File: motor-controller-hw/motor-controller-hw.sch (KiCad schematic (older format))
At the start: 37 parts, among them J101 CAN, J102 Throttle, J103 Motor T, J104 Tran T, J105 USB_B_Micro, J106 Extra IO, J107 Hall Sensors, J108 CAN_DBG, J109 ABN Encoder, J110 SPI_DBG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

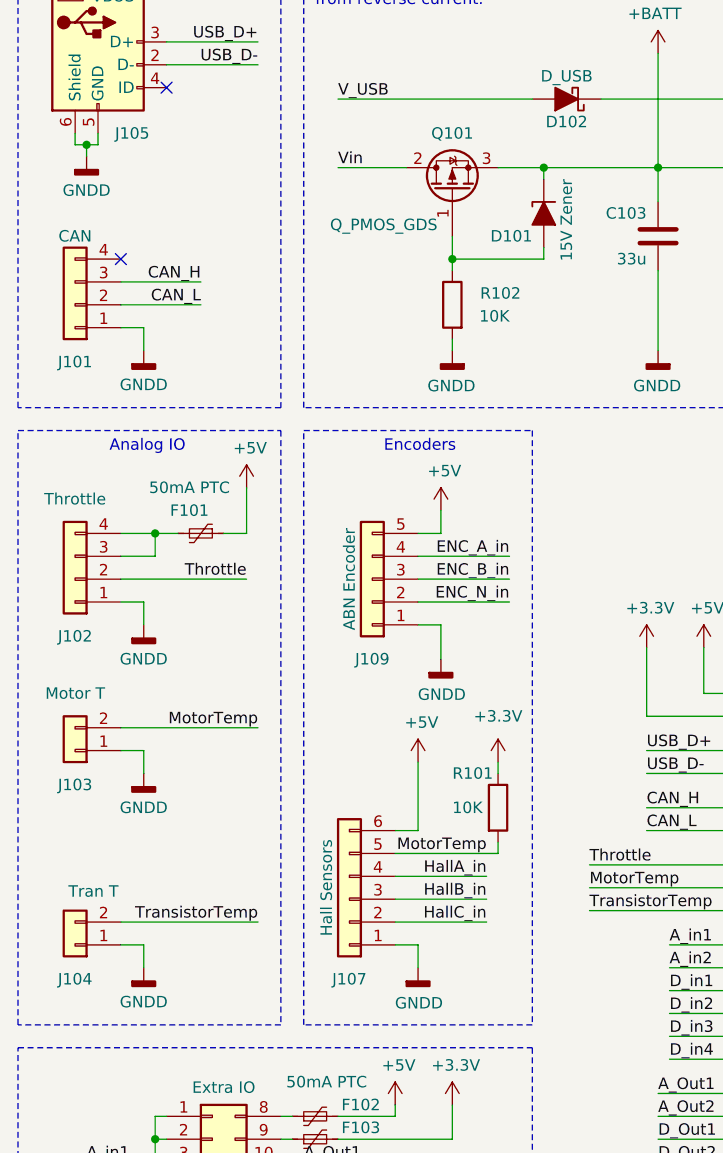
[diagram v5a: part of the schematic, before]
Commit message: PCB rev 1.1 -Fixed the TMC4671 footprint (use the Digi-Key layout) -Fixed the USB pull up issue for using the DFU bootloader -Fixed the orientation of the Hall sensor connector -Added a PTC on the hall effect sensor line -Added a 5v jumper for the CAN port
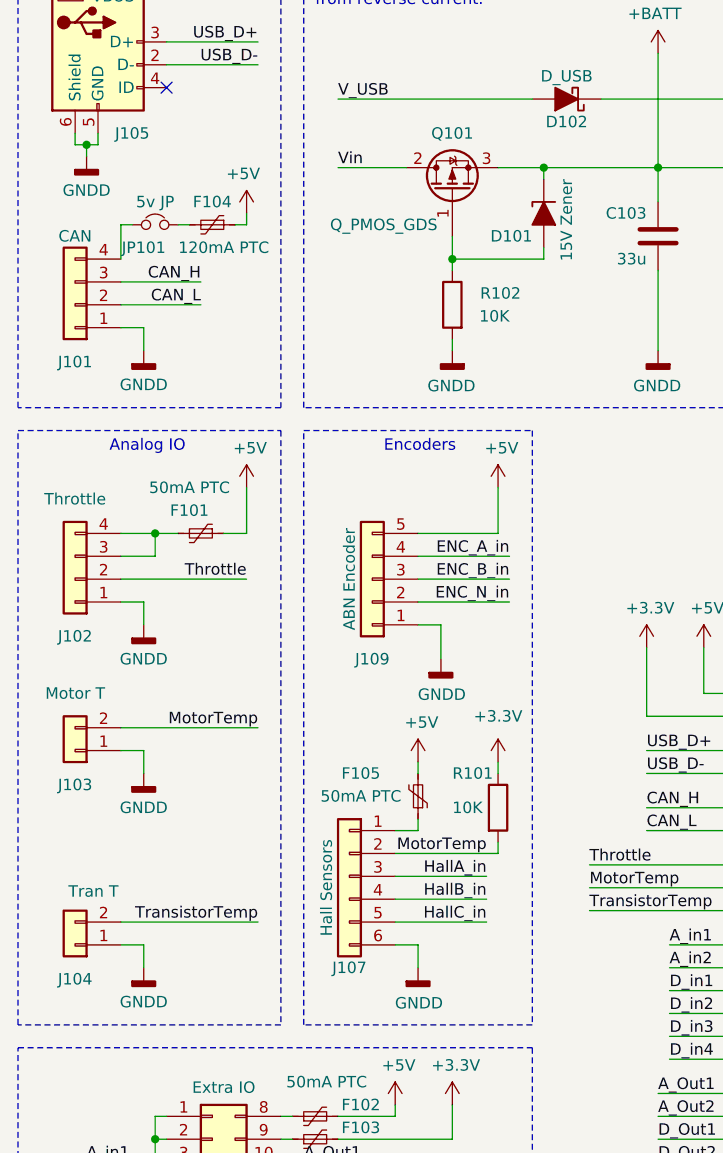
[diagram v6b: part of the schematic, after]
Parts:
- added F104: 120mA PTC, Fuse:Fuse_0603_1608Metric_Pad1.05x0.95mm_HandSolder, symbol MotorControllerParts:Polyfuse_Small
- added F105: 50mA PTC, Fuse:Fuse_0603_1608Metric_Pad1.05x0.95mm_HandSolder, symbol MotorControllerParts:Polyfuse_Small
- added JP101: 5v JP, Connector_PinHeader_2.54mm:PinHeader_1x02_P2.54mm_Vertical, symbol MotorControllerParts:Jumper_NC_Small
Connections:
- net +5V: now also F104.1, F105.2; no longer J107.6 (Pin_6)
- net GNDD: now also J107.6 (Pin_6); no longer J107.1 (Pin_1)
- net HallA_in: now also J107.3 (Pin_3); no longer J107.4 (Pin_4)
- net HallB_in: now also J107.4 (Pin_4); no longer J107.3 (Pin_3)
- net HallC_in: now also J107.5 (Pin_5); no longer J107.2 (Pin_2)
- net MotorTemp: now also J107.2 (Pin_2); no longer J107.5 (Pin_5)
- net at J101.4 (Pin_4): now also JP101.1
- new net: F105.1, J107.1 (Pin_1)
- new net: F104.2, JP101.2
- no-connect marks 22 -> 21
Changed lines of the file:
@@
 Wire Wire Line
 	1600 1300 1200 1300
-NoConn ~ 1000 2150
 $Comp
 L MotorControllerParts:Polyfuse_Small F101
@@
 L MotorControllerParts:Conn_01x06 J107
 U 1 1 5BF7BB3E
-P 2000 4950
-F 0 "J107" H 2000 5300 50  0000 C CNN
-F 1 "Hall Sensors" V 2100 4900 50  0000 C CNN
-F 2 "supermileage_footprints:MICRO_JST_6" H 2000 4950 50  0001 C CNN
-F 3 "http://www.jst-mfg.com/product/pdf/eng/ePH.pdf" H 2000 4950 50  0001 C CNN
-F 4 "455-1708-ND" H 2000 4950 50  0001 C CNN "Digi-key#"
-	1    2000 4950
-	-1   0    0    1
+P 2000 4850
+F 0 "J107" H 2000 4450 50  0000 C CNN
+F 1 "Hall Sensors" V 2100 4800 50  0000 C CNN
+F 2 "supermileage_footprints:MICRO_JST_6" H 2000 4850 50  0001 C CNN
+F 3 "http://www.jst-mfg.com/product/pdf/eng/ePH.pdf" H 2000 4850 50  0001 C CNN
+F 4 "455-1708-ND" H 2000 4850 50  0001 C CNN "Digi-key#"
+	1    2000 4850
+	-1   0    0    -1
 $EndComp
 $Comp
@@
 	1    0    0    -1
 $EndComp
-Wire Wire Line
-	2300 4350 2300 4650
 Wire Wire Line
 	2300 4650 2200 4650
@@
 L MotorControllerParts:+5V #PWR0118
 U 1 1 5E78636F
-P 2400 3250
-F 0 "#PWR0118" H 2400 3100 50  0001 C CNN
-F 1 "+5V" H 2415 3423 50  0000 C CNN
-F 2 "" H 2400 3250 50  0001 C CNN
-F 3 "" H 2400 3250 50  0001 C CNN
-	1    2400 3250
-	1    0    0    -1
-$EndComp
-Wire Wire Line
-	2400 3250 2400 3350
-Wire Wire Line
-	2400 3350 2300 3350
+P 2650 3150
+F 0 "#PWR0118" H 2650 3000 50  0001 C CNN
+F 1 "+5V" H 2665 3323 50  0000 C CNN
+F 2 "" H 2650 3150 50  0001 C CNN
+F 3 "" H 2650 3150 50  0001 C CNN
+	1    2650 3150
+	1    0    0    -1
+$EndComp
 Wire Wire Line
 	2400 3900 2400 3750
@@
 Power Status LEDs
 NoConn ~ 9900 1750
+$Comp
+L MotorControllerParts:Polyfuse_Small F104
+U 1 1 5CA283F1
+P 1400 2000
+F 0 "F104" V 1300 2000 50  0000 C CNN
+F 1 "120mA PTC" V 1500 2050 50  0000 C CNN
+F 2 "Fuse:Fuse_0603_1608Metric_Pad1.05x0.95mm_HandSolder" H 1450 1800 50  0001 L CNN
+F 3 "https://belfuse.com/resources/CircuitProtection/datasheets/0ZCM%20Nov2016.pdf" H 1400 2000 50  0001 C CNN
+F 4 "507-1819-1-ND" H 1400 2000 50  0001 C CNN "Digi-key#"
+	1    1400 2000
+	0    1    1    0
+$EndComp
+$Comp
+L MotorControllerParts:+5V #PWR0147
+U 1 1 5CA3E631
+P 1550 1950
+F 0 "#PWR0147" H 1550 1800 50  0001 C CNN
+F 1 "+5V" H 1565 2123 50  0000 C CNN
+F 2 "" H 1550 1950 50  0001 C CNN
+F 3 "" H 1550 1950 50  0001 C CNN
+	1    1550 1950
+	-1   0    0    -1
+$EndComp
+Wire Wire Line
+	1550 1950 1550 2000
+$Comp
+L MotorControllerParts:Polyfuse_Small F105
+U 1 1 5CA9863C
+P 2300 4500
+F 0 "F105" H 2550 4400 50  0000 C CNN
+F 1 "50mA PTC" H 2550 4500 50  0000 C CNN
+F 2 "Fuse:Fuse_0603_1608Metric_Pad1.05x0.95mm_HandSolder" H 2350 4300 50  0001 L CNN
+F 3 "https://belfuse.com/resources/CircuitProtection/datasheets/0ZCM%20Nov2016.pdf" H 2300 4500 50  0001 C CNN
+F 4 "507-1816-1-ND" H 2300 4500 50  0001 C CNN "Digi-key#"
+	1    2300 4500
+	-1   0    0    1
+$EndComp
+Wire Wire Line
+	2650 3350 2650 3150
+$Comp
+L MotorControllerParts:Jumper_NC_Small JP?
+U 1 1 5CBA3D24
+P 1150 2000
+AR Path="/5BB2528B/5CBA3D24" Ref="JP?"  Part="1"
+AR Path="/5CBA3D24" Ref="JP101"  Part="1"
+F 0 "JP101" H 1100 1900 50  0000 C CNN
+F 1 "5v JP" H 1150 2100 50  0000 C CNN
+F 2 "Connector_PinHeader_2.54mm:PinHeader_1x02_P2.54mm_Vertical" H 1150 2000 50  0001 C CNN
+F 3 "https://media.digikey.com/PDF/Data%20Sheets/Sullins%20PDFs/xRxCzzzSxxN-RC_ST_11635-B.pdf" H 1150 2000 50  0001 C CNN
+F 4 "S1212EC-02-ND" H -10850 -350 50  0001 C CNN "Digi-key#"
+	1    1150 2000
+	1    0    0    -1
+$EndComp
+Wire Wire Line
+	1500 2000 1550 2000
+Wire Wire Line
+	1300 2000 1250 2000
+Wire Wire Line
+	1000 2150 1000 2000
+Wire Wire Line
+	1000 2000 1050 2000
+Wire Wire Line
+	2300 3350 2650 3350
+Wire Wire Line
+	2300 4600 2300 4650
+Wire Wire Line
+	2300 4400 2300 4350
 $EndSCHEMATC
